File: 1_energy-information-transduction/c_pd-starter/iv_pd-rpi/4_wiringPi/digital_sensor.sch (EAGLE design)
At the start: 3 parts

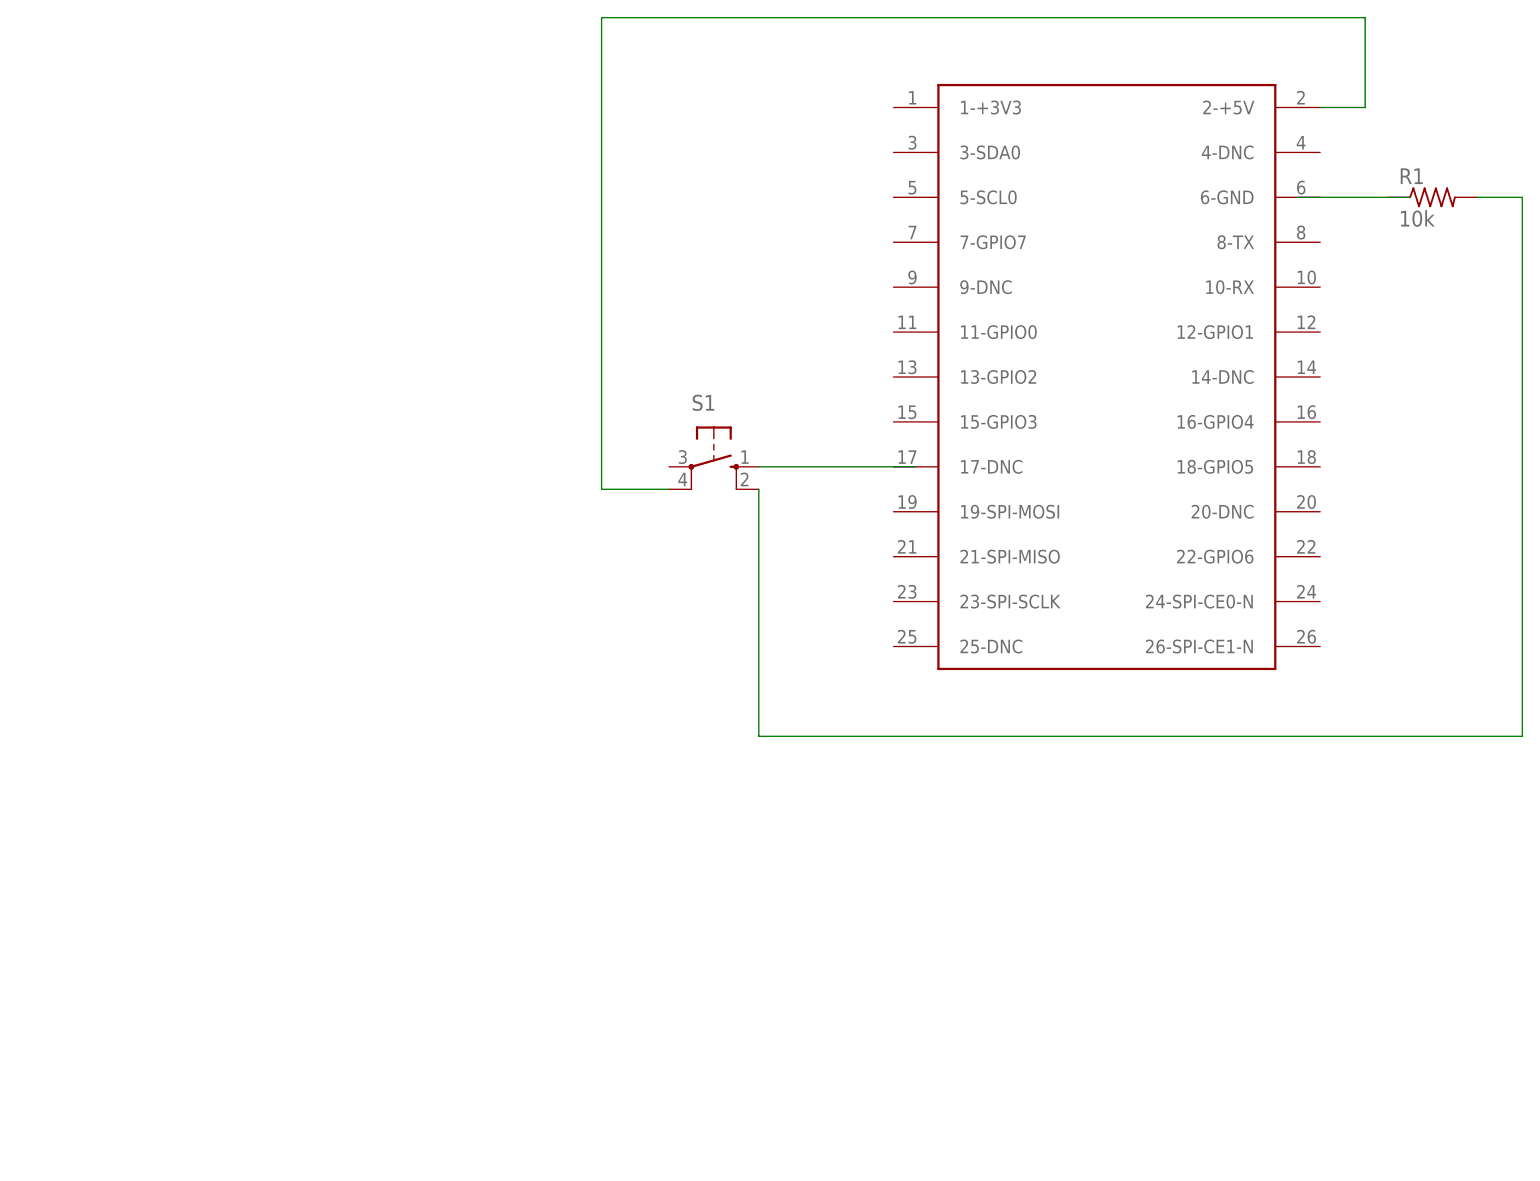
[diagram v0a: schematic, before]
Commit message: Add diagrams for first WiringPi examples.
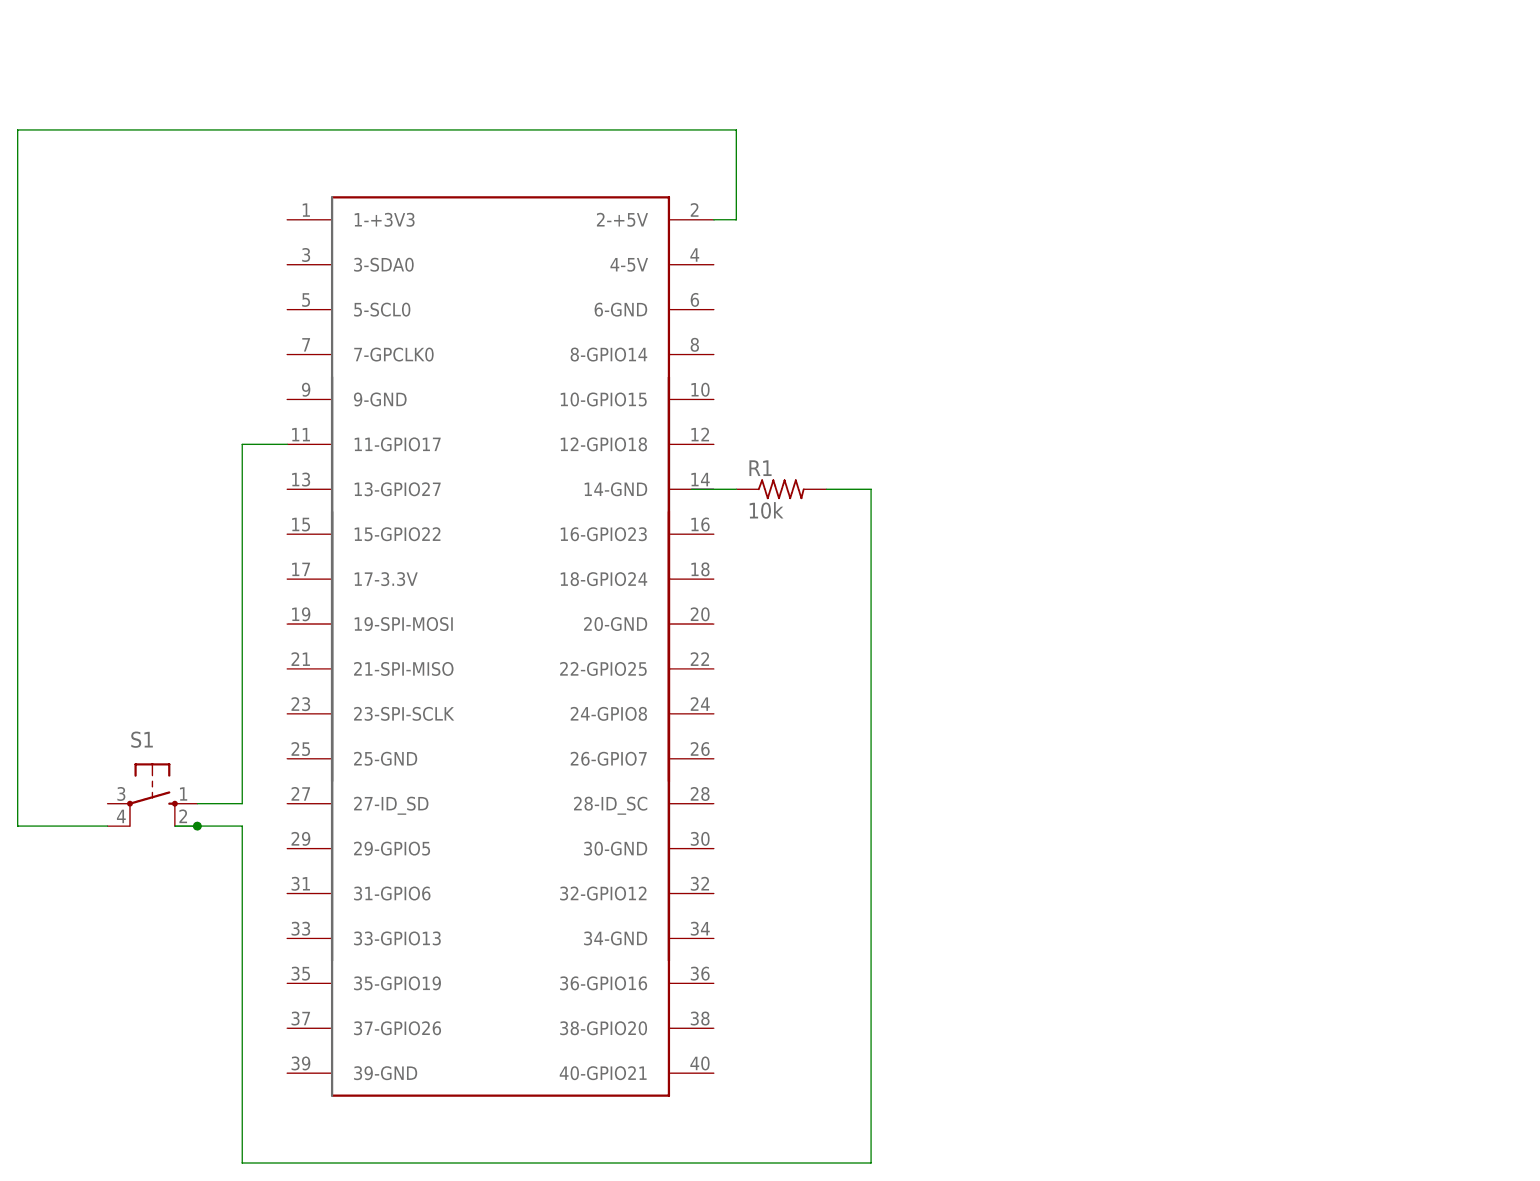
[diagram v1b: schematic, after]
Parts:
- U$1: device RaspberryPi:RASPBERRY-PI -> aliEagleLib:RASPBERRY-PI
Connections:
- removed net N$1 (its old number): S1.S
- new net N$2: R1.1
- new net N$3: S1.S, U$1.11-GPIO17
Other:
- moved on the sheet: R1, S1
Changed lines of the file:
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@@
 </classes>
 <parts>
-<part name="U$1" library="RaspberryPi" deviceset="RASPBERRY-PI" device=""/>
 <part name="S1" library="adafruit" deviceset="40-XX" device="-ROUND"/>
 <part name="R1" library="adafruit" deviceset="R-US_" device="0207/12" value="10k"/>
+<part name="U$1" library="aliEagleLib" deviceset="RASPBERRY-PI" device=""/>
 </parts>
 <sheets>
@@
 </plain>
 <instances>
-<instance part="U$1" gate="G$1" x="68.58" y="15.24"/>
-<instance part="S1" gate="1" x="27.94" y="25.4" rot="R270"/>
-<instance part="R1" gate="G$1" x="109.22" y="55.88"/>
+<instance part="S1" gate="1" x="-35.56" y="-12.7" rot="R270"/>
+<instance part="R1" gate="G$1" x="35.56" y="22.86"/>
+<instance part="U$1" gate="G$1" x="5.08" y="0"/>
 </instances>
 <busses>
@@
 <net name="N$1" class="0">
 <segment>
-<pinref part="S1" gate="1" pin="S"/>
-<wire x1="33.02" y1="25.4" x2="50.8" y2="25.4" width="0.1524" layer="91"/>
+<pinref part="S1" gate="1" pin="P1"/>
+<wire x1="-40.64" y1="-15.24" x2="-50.8" y2="-15.24" width="0.1524" layer="91"/>
+<wire x1="-50.8" y1="-15.24" x2="-50.8" y2="63.5" width="0.1524" layer="91"/>
+<wire x1="-50.8" y1="63.5" x2="30.48" y2="63.5" width="0.1524" layer="91"/>
+<wire x1="30.48" y1="63.5" x2="30.48" y2="53.34" width="0.1524" layer="91"/>
+<pinref part="U$1" gate="G$1" pin="2-+5V"/>
+<wire x1="30.48" y1="53.34" x2="27.94" y2="53.34" width="0.1524" layer="91"/>
 </segment>
 </net>
 <net name="N$2" class="0">
 <segment>
-<wire x1="93.98" y1="55.88" x2="106.68" y2="55.88" width="0.1524" layer="91"/>
+<pinref part="R1" gate="G$1" pin="1"/>
+<wire x1="25.4" y1="22.86" x2="30.48" y2="22.86" width="0.1524" layer="91"/>
+</segment>
+</net>
+<net name="N$4" class="0">
+<segment>
+<pinref part="S1" gate="1" pin="S1"/>
+<wire x1="-30.48" y1="-15.24" x2="-33.02" y2="-15.24" width="0.1524" layer="91"/>
+<wire x1="-30.48" y1="-15.24" x2="-25.4" y2="-15.24" width="0.1524" layer="91"/>
+<wire x1="-25.4" y1="-15.24" x2="-25.4" y2="-53.34" width="0.1524" layer="91"/>
+<junction x="-30.48" y="-15.24"/>
+<pinref part="R1" gate="G$1" pin="2"/>
+<wire x1="45.72" y1="22.86" x2="40.64" y2="22.86" width="0.1524" layer="91"/>
+<wire x1="-25.4" y1="-53.34" x2="45.72" y2="-53.34" width="0.1524" layer="91"/>
+<wire x1="45.72" y1="-53.34" x2="45.72" y2="22.86" width="0.1524" layer="91"/>
 </segment>
 </net>
 <net name="N$3" class="0">
 <segment>
-<pinref part="R1" gate="G$1" pin="2"/>
-<wire x1="114.3" y1="55.88" x2="119.38" y2="55.88" width="0.1524" layer="91"/>
-<wire x1="119.38" y1="55.88" x2="119.38" y2="-5.08" width="0.1524" layer="91"/>
-<pinref part="S1" gate="1" pin="S1"/>
-<wire x1="119.38" y1="-5.08" x2="33.02" y2="-5.08" width="0.1524" layer="91"/>
-<wire x1="33.02" y1="-5.08" x2="33.02" y2="22.86" width="0.1524" layer="91"/>
+<pinref part="S1" gate="1" pin="S"/>
+<wire x1="-30.48" y1="-12.7" x2="-25.4" y2="-12.7" width="0.1524" layer="91"/>
+<wire x1="-25.4" y1="-12.7" x2="-25.4" y2="27.94" width="0.1524" layer="91"/>
+<pinref part="U$1" gate="G$1" pin="11-GPIO17"/>
+<wire x1="-25.4" y1="27.94" x2="-20.32" y2="27.94" width="0.1524" layer="91"/>
 </segment>
 </net>
-<net name="N$4" class="0">
-<segment>
-<pinref part="S1" gate="1" pin="P1"/>
-<wire x1="22.86" y1="22.86" x2="15.24" y2="22.86" width="0.1524" layer="91"/>
-<wire x1="15.24" y1="22.86" x2="15.24" y2="76.2" width="0.1524" layer="91"/>
-<wire x1="15.24" y1="76.2" x2="101.6" y2="76.2" width="0.1524" layer="91"/>
-<wire x1="101.6" y1="76.2" x2="101.6" y2="66.04" width="0.1524" layer="91"/>
-<pinref part="U$1" gate="G$1" pin="2-+5V"/>
-<wire x1="101.6" y1="66.04" x2="96.52" y2="66.04" width="0.1524" layer="91"/>
-</segment>
-</net>
